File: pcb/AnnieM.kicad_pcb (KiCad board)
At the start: 2 copper layers, 25.7 x 57.4 mm, 24 parts, among them J1 NRG200P, J2 NRG400, J3 SOLAR, U1 LMT86, U3 LM393

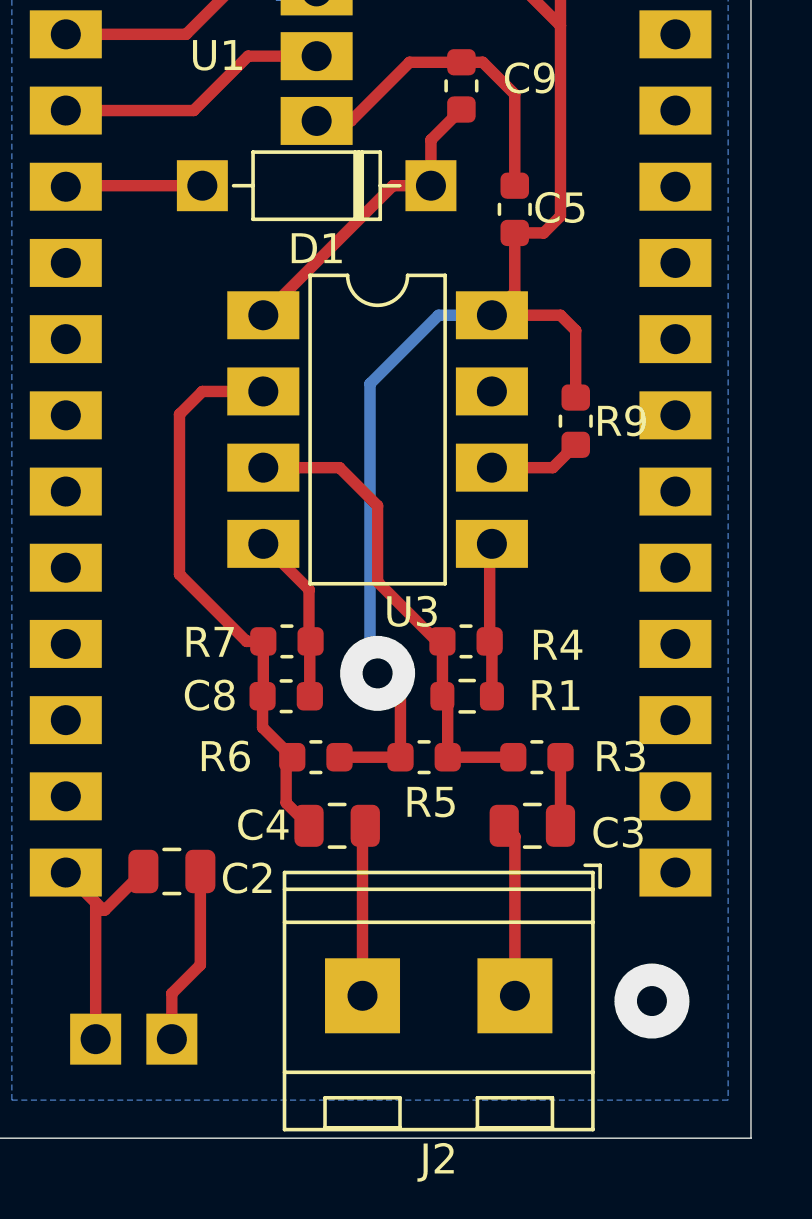
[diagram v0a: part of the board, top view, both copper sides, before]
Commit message: added pull up to schematic
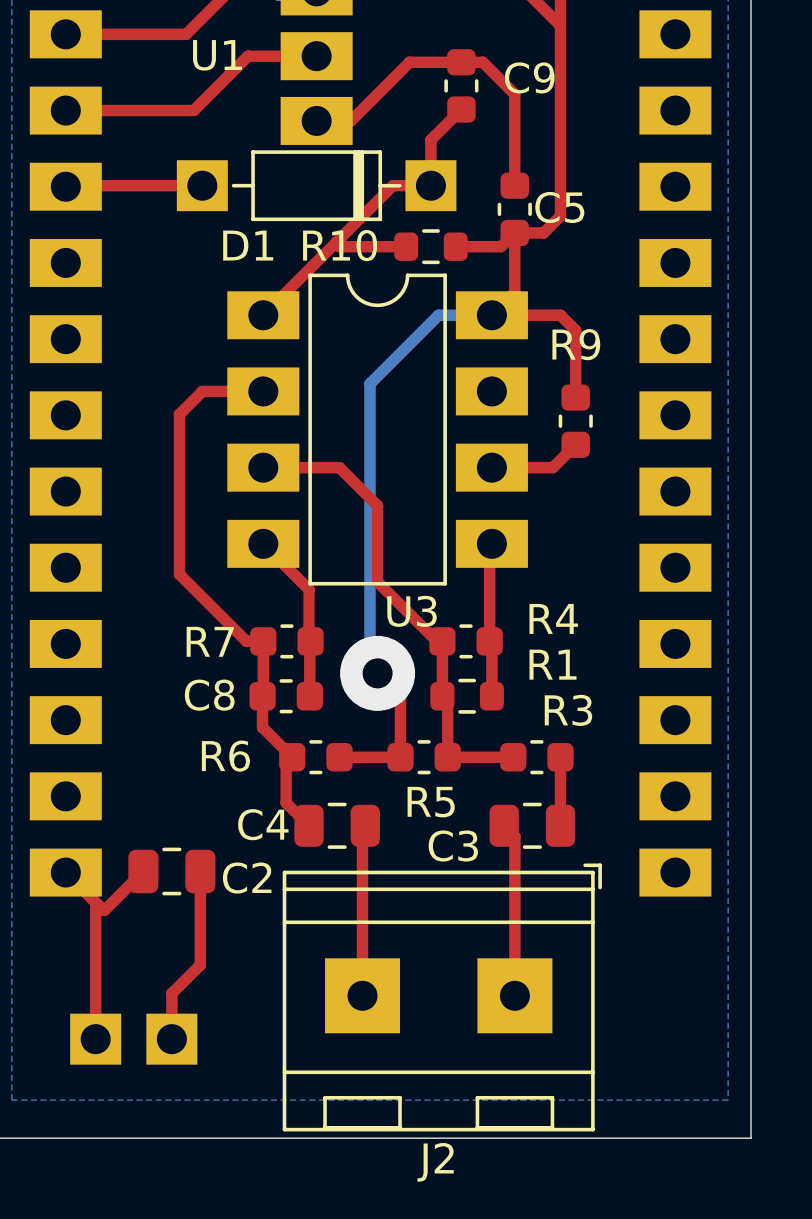
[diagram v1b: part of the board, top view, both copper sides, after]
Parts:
- added R10: 100K, Resistor_SMD:R_0603_1608Metric, F.Cu at (34.2, 50.8)
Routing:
- net Net-(C9-Pad2): track 10.3 -> 12.7 mm
- net VCC: track 60.7 -> 62.8 mm
- net (no net): vias 1 -> 0
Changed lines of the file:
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@@
     (property "Sheetname" "")
     (attr smd)
-    (fp_text reference "R3" (at 2.794 0) (layer "F.SilkS")
+    (fp_text reference "R3" (at 1.0415 -1.524) (layer "F.SilkS")
       (effects (font (size 1 1) (thickness 0.15)))
     )
@@
     (property "Sheetname" "")
     (attr smd)
-    (fp_text reference "R4" (at -3.0415 -0.15) (layer "F.SilkS")
+    (fp_text reference "R4" (at -2.8945 0.711) (layer "F.SilkS")
       (effects (font (size 1 1) (thickness 0.15)))
     )
@@
     (property "Sheetname" "")
     (attr smd)
-    (fp_text reference "R9" (at -0.0255 1.524) (layer "F.SilkS")
+    (fp_text reference "R9" (at 2.5145 0) (layer "F.SilkS")
       (effects (font (size 1 1) (thickness 0.15)))
     )
@@
     (property "Sheetname" "")
     (attr smd)
-    (fp_text reference "C3" (at -2.8725 -0.254) (layer "F.SilkS")
+    (fp_text reference "C3" (at 2.6185 -0.71) (layer "F.SilkS")
       (effects (font (size 1 1) (thickness 0.15)))
     )
@@
     (property "Sheetname" "")
     (attr smd)
-    (fp_text reference "R1" (at -2.953 0) (layer "F.SilkS")
+    (fp_text reference "R1" (at -2.857 1.016) (layer "F.SilkS")
       (effects (font (size 1 1) (thickness 0.15)))
     )
@@
     )
   )
+  (footprint "Resistor_SMD:R_0603_1608Metric" (layer "F.Cu")
+    (at 34.186 50.832)
+    (descr "Resistor SMD 0603 (1608 Metric), square (rectangular) end terminal, IPC_7351 nominal, (Body size source: IPC-SM-782 page 72, https://www.pcb-3d.com/wordpress/wp-content/uploads/ipc-sm-782a_amendment_1_and_2.pdf), generated with kicad-footprint-generator")
+    (tags "resistor")
+    (property "Sheetfile" "AnnieM.kicad_sch")
+    (property "Sheetname" "")
+    (attr smd)
+    (fp_text reference "R10" (at -3.048 0) (layer "F.SilkS")
+      (effects (font (size 1 1) (thickness 0.15)))
+    )
+    (fp_text value "100K" (at 0 1.43) (layer "F.Fab")
+      (effects (font (size 1 1) (thickness 0.15)))
+    )
+    (fp_text user "${REFERENCE}" (at 0 0) (layer "F.Fab")
+      (effects (font (size 0.4 0.4) (thickness 0.06)))
+    )
+    (fp_line (start -0.237258 0.5225) (end 0.237258 0.5225) (layer "F.SilkS") (width 0.12))
+    (fp_line (start -0.237258 -0.5225) (end 0.237258 -0.5225) (layer "F.SilkS") (width 0.12))
+    (fp_line (start -1.48 -0.73) (end 1.48 -0.73) (layer "F.CrtYd") (width 0.05))
+    (fp_line (start -1.48 0.73) (end -1.48 -0.73) (layer "F.CrtYd") (width 0.05))
+    (fp_line (start 1.48 0.73) (end -1.48 0.73) (layer "F.CrtYd") (width 0.05))
+    (fp_line (start 1.48 -0.73) (end 1.48 0.73) (layer "F.CrtYd") (width 0.05))
+    (fp_line (start 0.8 0.4125) (end -0.8 0.4125) (layer "F.Fab") (width 0.1))
+    (fp_line (start 0.8 -0.4125) (end 0.8 0.4125) (layer "F.Fab") (width 0.1))
+    (fp_line (start -0.8 -0.4125) (end 0.8 -0.4125) (layer "F.Fab") (width 0.1))
+    (fp_line (start -0.8 0.4125) (end -0.8 -0.4125) (layer "F.Fab") (width 0.1))
+    (pad "1" smd roundrect (at -0.825 0) (size 0.8 0.95) (layers "F.Cu" "F.Paste" "F.Mask") (roundrect_rratio 0.25)
+      (net 11 "Net-(C9-Pad2)") (pintype "passive"))
+    (pad "2" smd roundrect (at 0.825 0) (size 0.8 0.95) (layers "F.Cu" "F.Paste" "F.Mask") (roundrect_rratio 0.25)
+      (net 9 "VCC") (pintype "passive"))
+    (model "${KICAD6_3DMODEL_DIR}/Resistor_SMD.3dshapes/R_0603_1608Metric.wrl"
+      (offset (xyz 0 0 0))
+      (scale (xyz 1 1 1))
+      (rotate (xyz 0 0 0))
+    )
+  )
   (footprint "Diode_THT:D_DO-35_SOD27_P7.62mm_Horizontal" (layer "F.Cu")
     (at 34.186 48.8 180)
@@
     (property "Sheetname" "")
     (attr through_hole)
-    (fp_text reference "D1" (at 3.81 -2.12) (layer "F.SilkS")
+    (fp_text reference "D1" (at 6.096 -2.032) (layer "F.SilkS")
       (effects (font (size 1 1) (thickness 0.15)))
     )
@@
   (gr_line (start 44.854 80.55) (end 19.2 80.55) (layer "Edge.Cuts") (width 0.05))
   (gr_line (start 44.854 23.146) (end 44.854 80.55) (layer "Edge.Cuts") (width 0.05))
-  (via (at 41.552 75.978) (size 2.5) (drill 1) (layers "F.Cu" "B.Cu") (free) (net 0))
   (segment (start 38.504 67.85) (end 38.504 70.136) (width 0.381) (layer "F.Cu") (net 1))
   (segment (start 29.36 69.374) (end 29.36 68.053) (width 0.381) (layer "F.Cu") (net 2))
@@
   (segment (start 27.958 40.418) (end 27.958 41.82) (width 0.381) (layer "F.Cu") (net 8))
   (segment (start 38.504 53.118) (end 36.218 53.118) (width 0.381) (layer "F.Cu") (net 9))
+  (segment (start 36.523 50.832) (end 36.98 50.375) (width 0.381) (layer "F.Cu") (net 9))
   (segment (start 32.408 65.056) (end 33.17 65.818) (width 0.381) (layer "F.Cu") (net 9))
   (segment (start 33.17 65.818) (end 33.17 67.85) (width 0.381) (layer "F.Cu") (net 9))
   (segment (start 37.361 42.323) (end 38.504 43.466) (width 0.381) (layer "F.Cu") (net 9))
+  (segment (start 35.011 50.832) (end 36.523 50.832) (width 0.381) (layer "F.Cu") (net 9))
   (segment (start 38.504 43.466) (end 38.504 38.512) (width 0.381) (layer "F.Cu") (net 9))
   (segment (start 38.504 49.816) (end 38.504 43.466) (width 0.381) (layer "F.Cu") (net 9))
@@
   (segment (start 32.916 48.8) (end 34.186 48.8) (width 0.381) (layer "F.Cu") (net 11))
   (segment (start 34.186 47.276) (end 35.202 46.26) (width 0.381) (layer "F.Cu") (net 11))
-  (segment (start 28.598 53.118) (end 32.916 48.8) (width 0.381) (layer "F.Cu") (net 11))
+  (segment (start 31.138 50.832) (end 31.011 50.705) (width 0.381) (layer "F.Cu") (net 11))
+  (segment (start 31.011 50.705) (end 32.916 48.8) (width 0.381) (layer "F.Cu") (net 11))
+  (segment (start 33.361 50.832) (end 31.138 50.832) (width 0.381) (layer "F.Cu") (net 11))
   (segment (start 34.186 48.8) (end 34.186 47.276) (width 0.381) (layer "F.Cu") (net 11))
+  (segment (start 28.598 53.118) (end 31.011 50.705) (width 0.381) (layer "F.Cu") (net 11))
   (segment (start 26.278 46.294) (end 28.09 44.482) (width 0.381) (layer "F.Cu") (net 14))
   (segment (start 22.015 46.294) (end 26.278 46.294) (width 0.381) (layer "F.Cu") (net 14))

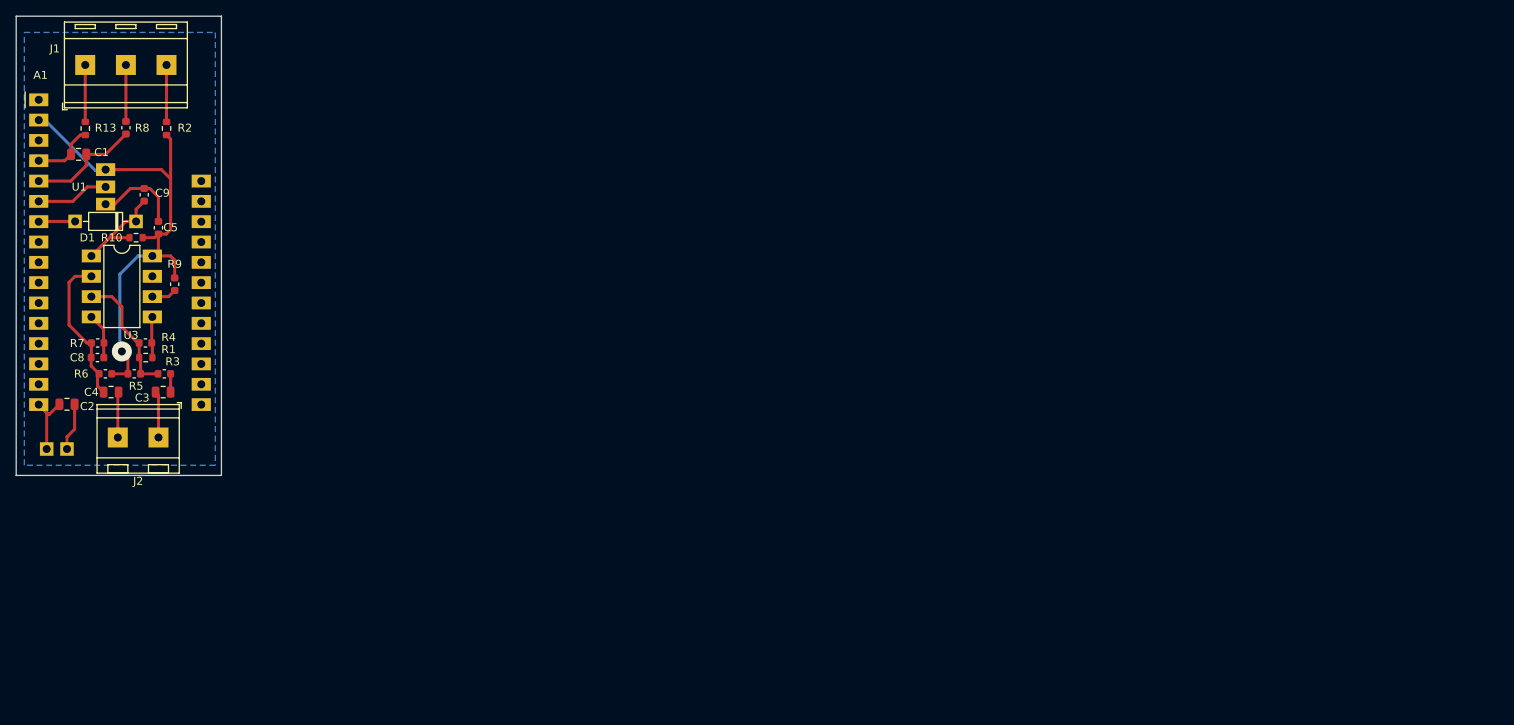
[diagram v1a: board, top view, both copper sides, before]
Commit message: Restarted pcb layout, added bme866 and Arducam 5MP
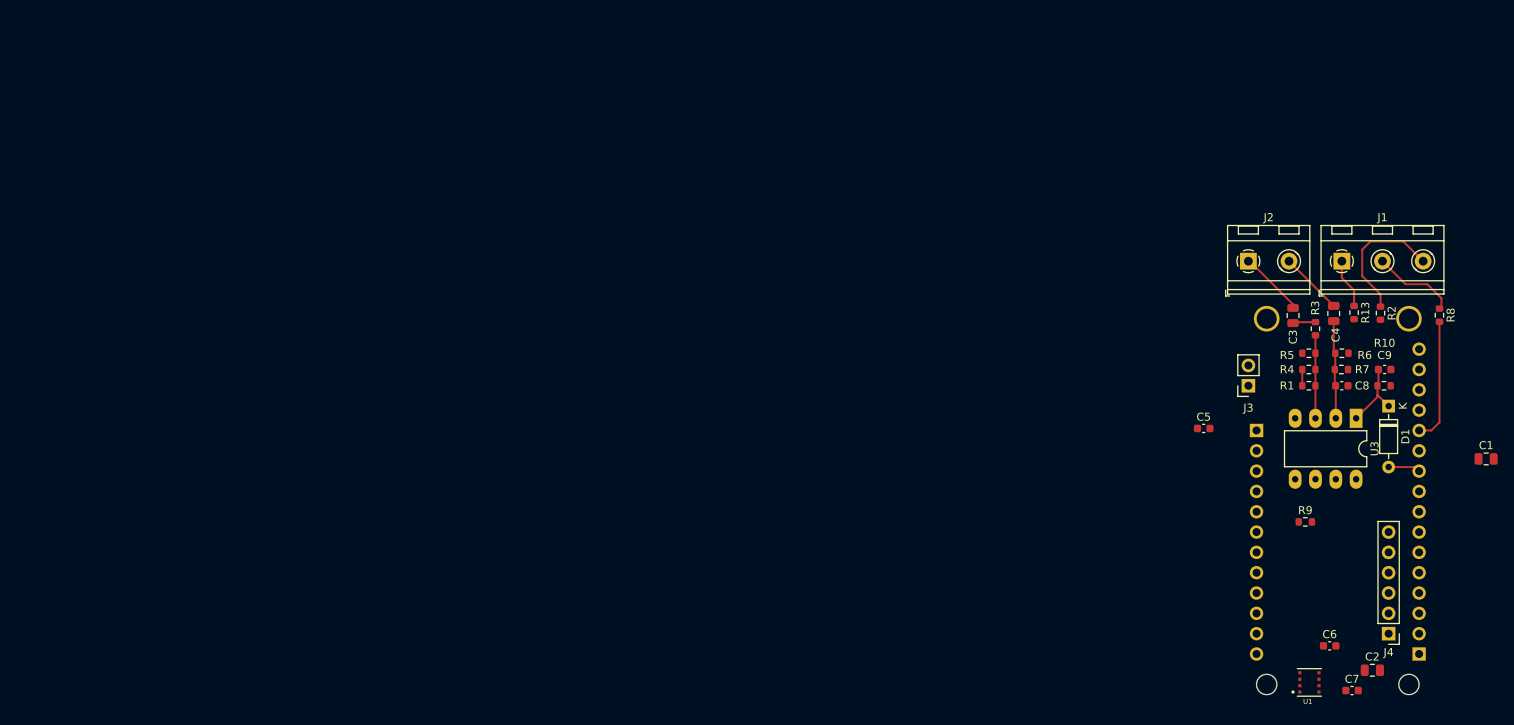
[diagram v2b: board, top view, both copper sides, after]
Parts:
- removed A1: Adafruit_Feather_Generic, Module:Adafruit_Feather
- added C6: 0.1uf, Capacitor_SMD:C_0603_1608Metric, F.Cu at (183.4, 101.9)
- added C7: 0.1uf, Capacitor_SMD:C_0603_1608Metric, F.Cu at (186.2, 107.4)
- added J4: ARDUCAM, Connector_PinHeader_2.54mm:PinHeader_1x06_P2.54mm_Vertical, F.Cu at (190.8, 100.3)
- added U2: ICARUS_IOT_BOARD_TH, ICARUS_IOT_BOARD_TH:MODULE_ICARUS_IOT_BOARD_TH, B.Cu at (184.4, 83.8)
- J1: footprint TerminalBlock_RND:TerminalBlock_RND_205-00288_1x03_P5.08mm_Horizontal -> TerminalBlock_RND:TerminalBlock_RND_205-00233_1x03_P5.08mm_Horizontal
- J3: moved to F.Cu
- U1: value LMT86 -> BME688; footprint Package_TO_SOT_THT:TO-92_Inline -> BME688:IC_BME688
- moved C1 180.0 mm to (202.9, 78.5)
- moved C2 166.5 mm to (188.7, 104.9), turned to 0 degrees
- moved R8 165.9 mm to (197.1, 60.5)
- moved U1 163.2 mm to (180.8, 106.4), turned to 180 degrees
- moved R13 160.3 mm to (186.4, 60.2)
- moved U3 159.4 mm to (186.7, 73.4), turned to -90 degrees
- moved J1 159.0 mm to (184.9, 53.8)
- moved D1 158.3 mm to (190.8, 71.9), turned to -90 degrees
- moved R10 157.1 mm to (190.2, 69.3)
- moved C9 156.6 mm to (190.3, 67.3), turned to 180 degrees
- moved C8 155.6 mm to (184.9, 69.3)
- moved R7 155.5 mm to (184.8, 67.3)
- moved R6 154.6 mm to (184.9, 65.3)
- moved R2 153.5 mm to (189.7, 60.3)
- moved C4 153.1 mm to (183.9, 60.3), turned to 90 degrees
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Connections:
- U1 pad 1: VCC -> GND
- U1 pad 2: TEMPERATURE -> VCC
- U1 pad 3: GND -> SDA
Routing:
- net VCC: track 62.8 -> 0.00 mm, vias 1 -> 0
- net GND: track 35.6 -> 2.03 mm
- net Net-(J1-Pad3): track 6.85 -> 17.1 mm
- net +10V: track 9.60 -> 0.00 mm
- net TEMPERATURE: track 9.11 -> 0.00 mm
- net Net-(C4-Pad1): track 18.8 -> 12.3 mm
- net Net-(R1-Pad2): track 15.5 -> 10.4 mm
- net Net-(J1-Pad2): track 6.80 -> 10.7 mm
- net Net-(C9-Pad2): track 12.7 -> 9.23 mm
- net Net-(R9-Pad1): track 3.11 -> 0.00 mm
- net Net-(C3-Pad2): track 6.07 -> 8.26 mm
- net Net-(C4-Pad2): track 5.83 -> 7.90 mm
- net DIRECTION: track 14.2 -> 15.5 mm
- net Net-(J1-Pad1): track 6.85 -> 6.24 mm
- net Net-(C3-Pad1): track 2.29 -> 2.84 mm
- removed copper zone on B.Cu, net GND
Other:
- board outline removed
- rule pad_to_mask_clearance: 0.051 -> 0
